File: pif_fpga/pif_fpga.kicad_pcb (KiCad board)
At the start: 2 copper layers, 35 x 41 mm, 61 parts, among them P1 CONN_02X20, P2 CONN_01X18, P3 CONN_01X06, P4 CONN_01X05, U1 Si5351A, U2 LCMXO2-2000HC, U3 STM32F070CBT6, U4 W25Q128JVPIQ, U5 74LVC1G14, Y1 25 MHz

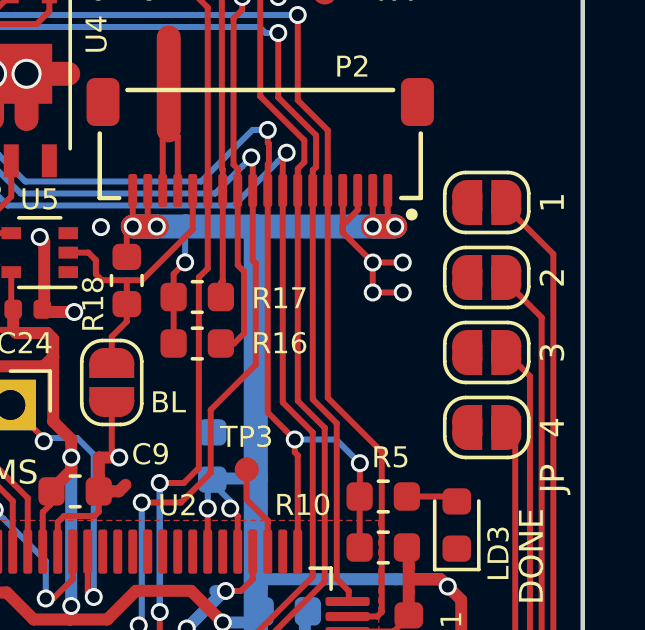
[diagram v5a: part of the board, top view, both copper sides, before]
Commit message: connected solder jumpers to GND
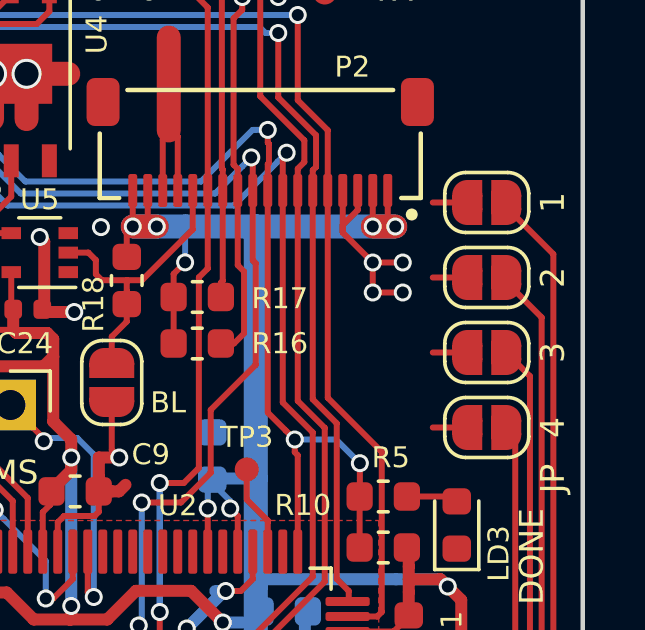
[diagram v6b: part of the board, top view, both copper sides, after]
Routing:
- net GND: track 210.2 -> 214.8 mm
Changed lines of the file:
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@@
     (thickness 1.6)
     (drawings 45)
-    (tracks 1189)
+    (tracks 1193)
     (zones 0)
     (modules 61)
@@
   )
   (setup
-    (last_trace_width 0.4)
+    (last_trace_width 0.2)
     (user_trace_width 0.16)
     (user_trace_width 0.4)
@@
   (segment (start 166.3 106.6) (end 166.5 106.8) (width 0.2) (layer F.Cu) (net 40))
   (segment (start 166.2 103.5) (end 166.2 106.6) (width 0.8) (layer F.Cu) (net 40))
+  (segment (start 176.15 109) (end 175 109) (width 0.2) (layer F.Cu) (net 40))
+  (segment (start 176.15 116.5) (end 175 116.5) (width 0.2) (layer F.Cu) (net 40))
+  (segment (start 176.15 114) (end 175 114) (width 0.2) (layer F.Cu) (net 40))
+  (segment (start 176.15 111.5) (end 175 111.5) (width 0.2) (layer F.Cu) (net 40))
   (segment (start 155.6 101.45) (end 156.5 101.45) (width 0.4) (layer F.Cu) (net 41))
   (segment (start 147.1 110.4) (end 148.225 111.525) (width 0.4) (layer F.Cu) (net 41))
